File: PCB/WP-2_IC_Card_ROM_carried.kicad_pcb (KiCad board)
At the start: 2 copper layers, 14.5 x 48.5 mm, 6 parts, among them J1 Conn_01x38_Female, U1 FLASH 256Kx8 5v Parallel, U2 FLASH 256Kx8 5v Parallel

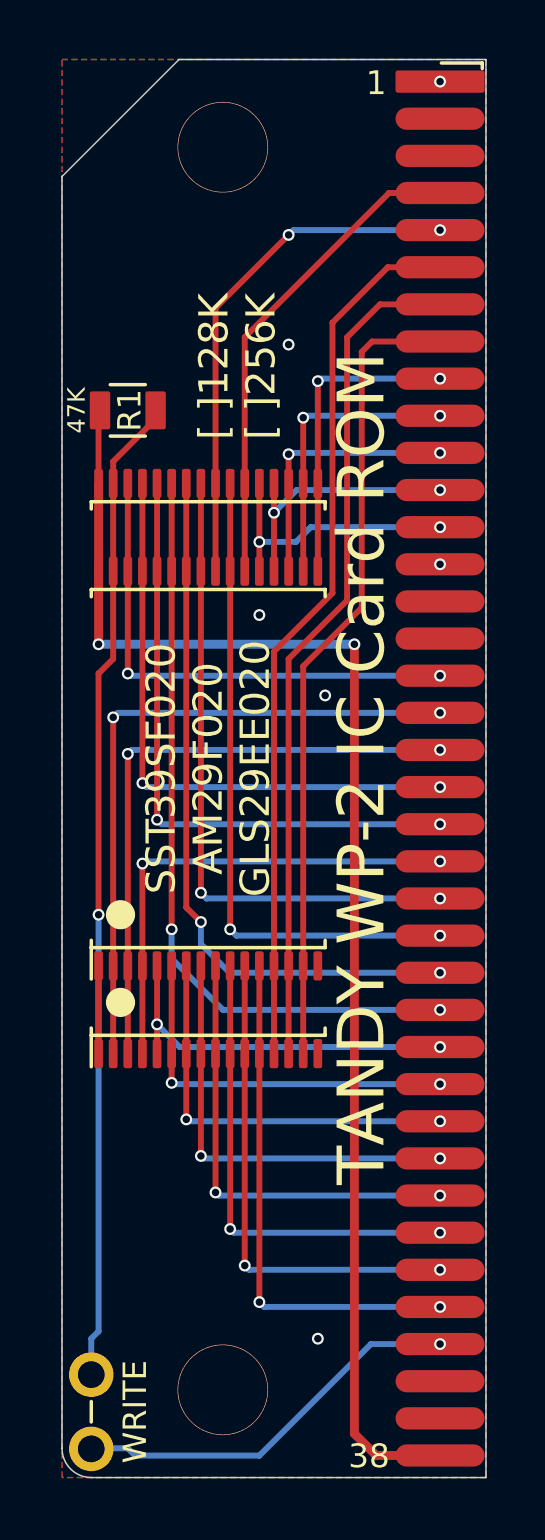
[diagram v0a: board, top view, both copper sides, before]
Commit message: fix ROM flash chip pinout
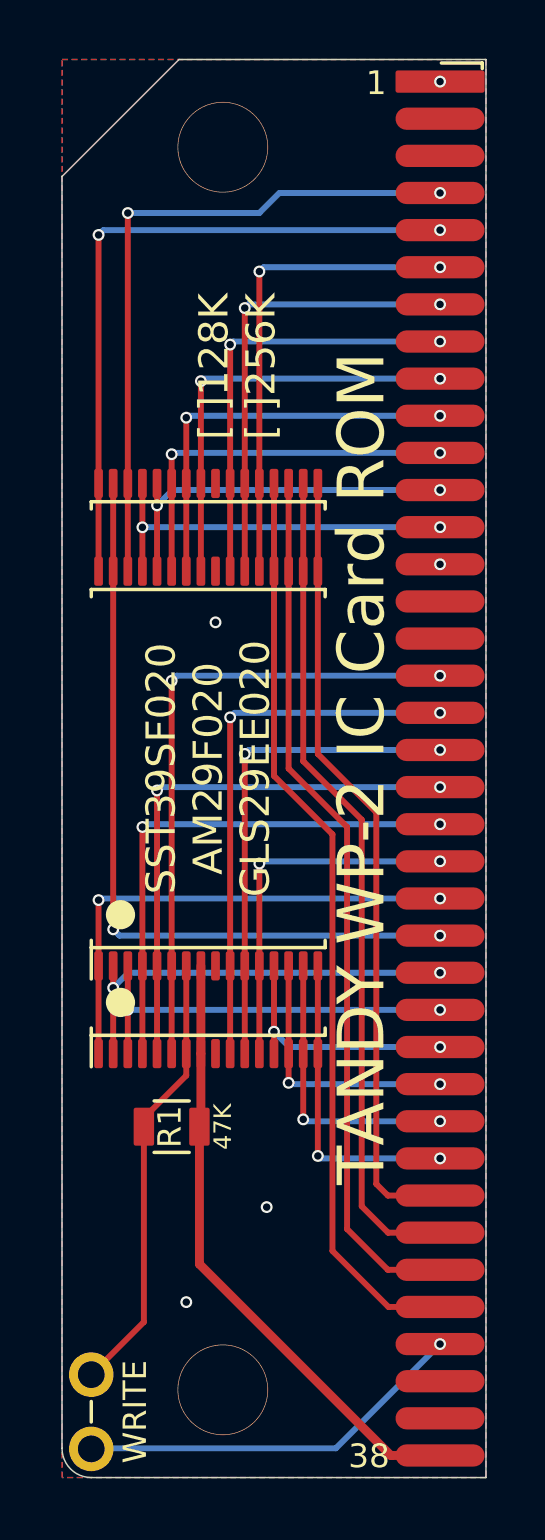
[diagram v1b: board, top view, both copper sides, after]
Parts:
- JP1: value WR_EN -> Write-Enable
- moved R1 24.5 mm to (148.0, 111.9), turned to 180 degrees
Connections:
- U1 pad 1: (no net) -> /A11
- U1 pad 10: /A2 -> /A16
- U1 pad 11: /A1 -> /A15
- U1 pad 12: /A0 -> /A12
- U1 pad 13: /D0 -> /A7
- U1 pad 14: /D1 -> /A6
- U1 pad 15: /D2 -> /A5
- U1 pad 16: GND -> /A4
- U1 pad 17: /D3 -> /A3
- U1 pad 18: /D4 -> /A2
- U1 pad 19: /D5 -> /A1
- U1 pad 2: /A16 -> /A9
- U1 pad 20: /D6 -> /A0
- U1 pad 21: /D7 -> /D0
- U1 pad 22: /~CE1 -> /D1
- U1 pad 23: /A10 -> /D2
- U1 pad 24: /~OE -> GND
- U1 pad 25: /A11 -> /D3
- U1 pad 26: /A9 -> /D4
- U1 pad 27: /A8 -> /D5
- U1 pad 28: /A13 -> /D6
- U1 pad 29: /A14 -> /D7
- U1 pad 3: /A15 -> /A8
- U1 pad 30: /A17 -> /~CE1
- U1 pad 31: /~WE -> /A10
- U1 pad 32: VDD -> /~OE
- U1 pad 4: /A12 -> /A13
- U1 pad 5: /A7 -> /A14
- U1 pad 6: /A6 -> /A17
- U1 pad 7: /A5 -> /~WE
- U1 pad 8: /A4 -> VDD
- U1 pad 9: /A3 -> (no net)
- U2 pad 1: (no net) -> /A11
- U2 pad 10: /A2 -> /A16
- U2 pad 11: /A1 -> /A15
- U2 pad 12: /A0 -> /A12
- U2 pad 13: /D0 -> /A7
- U2 pad 14: /D1 -> /A6
- U2 pad 15: /D2 -> /A5
- U2 pad 16: GND -> /A4
- U2 pad 17: /D3 -> /A3
- U2 pad 18: /D4 -> /A2
- U2 pad 19: /D5 -> /A1
- U2 pad 2: /A16 -> /A9
- U2 pad 20: /D6 -> /A0
- U2 pad 21: /D7 -> /D0
- U2 pad 22: /~CE1 -> /D1
- U2 pad 23: /A10 -> /D2
- U2 pad 24: /~OE -> GND
- U2 pad 25: /A11 -> /D3
- U2 pad 26: /A9 -> /D4
- U2 pad 27: /A8 -> /D5
- U2 pad 28: /A13 -> /D6
- U2 pad 29: /A14 -> /D7
- U2 pad 3: /A15 -> /A8
- U2 pad 30: /A17 -> /~CE1
- U2 pad 31: /~WE -> /A10
- U2 pad 32: VDD -> /~OE
- U2 pad 4: /A12 -> /A13
- U2 pad 5: /A7 -> /A14
- U2 pad 6: /A6 -> /A17
- U2 pad 7: /A5 -> /~WE
- U2 pad 8: /A4 -> VDD
- U2 pad 9: /A3 -> (no net)
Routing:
- net VDD: track 47.0 -> 21.2 mm, vias 2 -> 0
- net /~WE: track 33.9 -> 15.3 mm, vias 1 -> 0
- net /D0: track 30.3 -> 16.5 mm, vias 0 -> 2
- net /A0: track 17.7 -> 31.6 mm, vias 2 -> 0
- net /D1: track 29.0 -> 15.7 mm, vias 0 -> 2
- net /A1: track 17.0 -> 30.1 mm, vias 2 -> 0
- net /D2: track 27.7 -> 15.0 mm, vias 0 -> 2
- net /A8: track 26.2 -> 13.7 mm
- net /A2: track 16.2 -> 28.6 mm, vias 2 -> 0
- net /A3: track 15.5 -> 27.1 mm, vias 2 -> 0
- net /A9: track 24.5 -> 14.4 mm
- net /~CE1: track 16.7 -> 23.2 mm, vias 0 -> 2
- net /~OE: track 17.8 -> 23.2 mm
- net /A11: track 22.3 -> 17.0 mm
- net /A17: track 17.2 -> 22.0 mm
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
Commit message: fine-tune via-near-trace placements
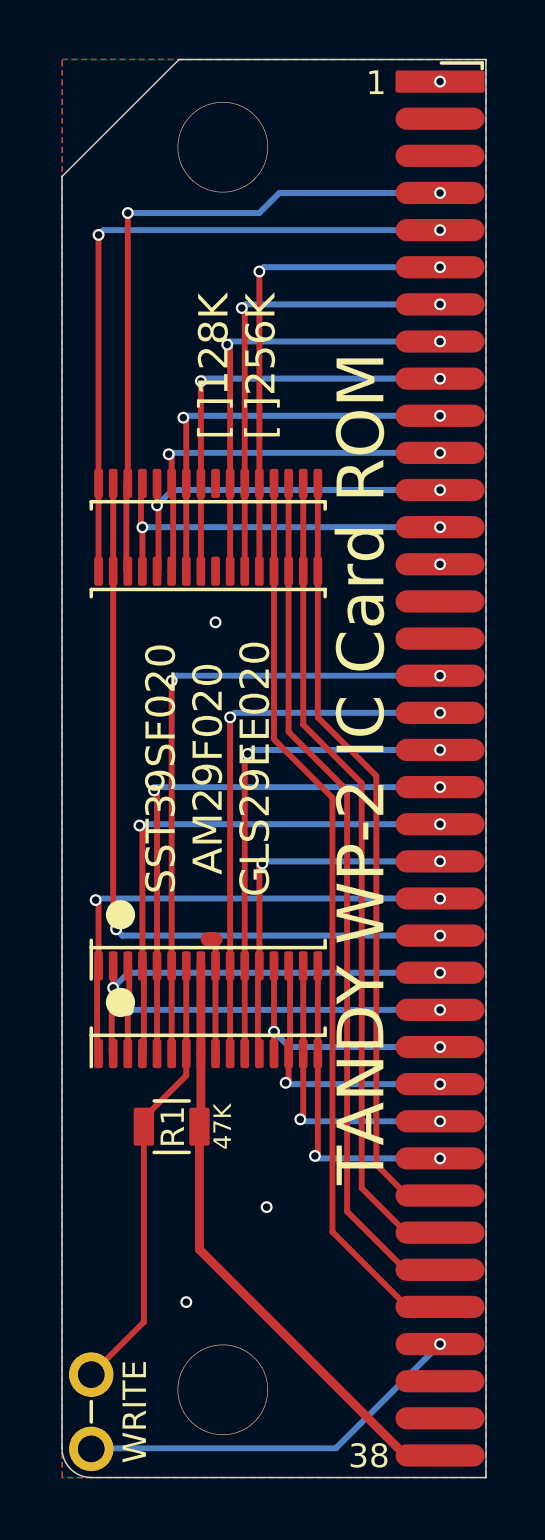
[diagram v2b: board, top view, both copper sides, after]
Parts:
- added NT1: Net-Tie_2, 0_LOCAL:Net_Tie_2p_8mil, F.Cu at (149.5, 105.9)
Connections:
- U1 pad 9: (no net) -> /A18
- U2 pad 9: (no net) -> /A18
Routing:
- net /A18: track 0.00 -> 3.00 mm

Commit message: increase via sizes and min soldermask width for PCBWAY
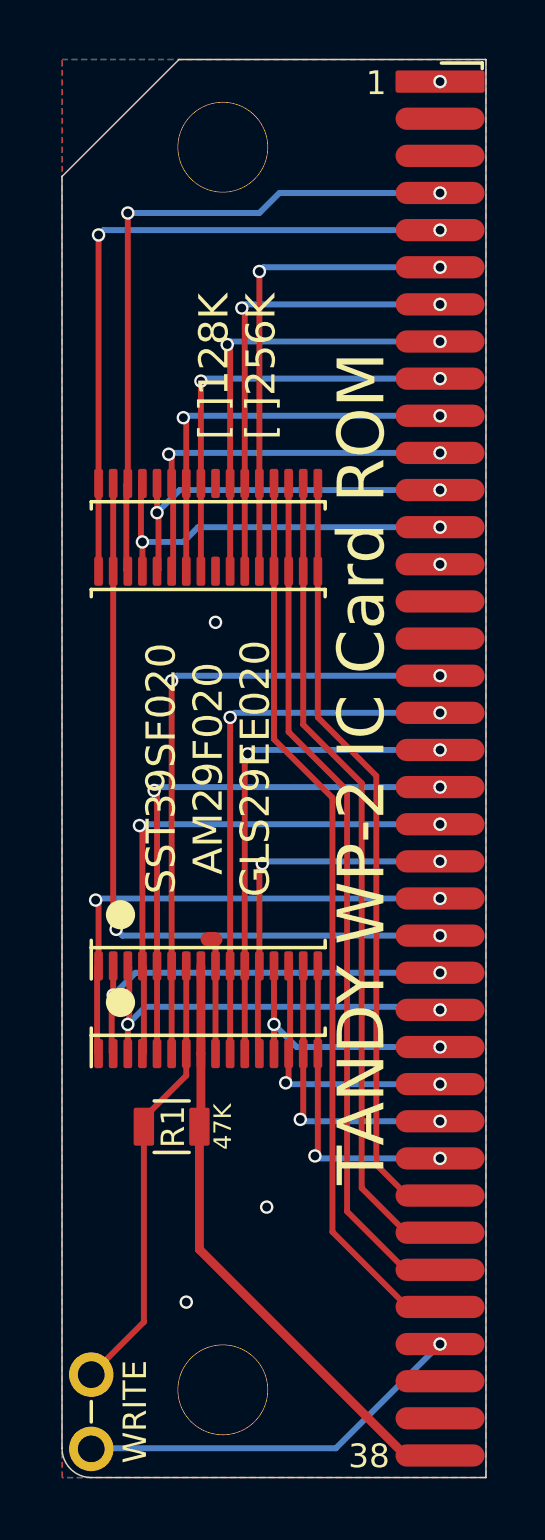
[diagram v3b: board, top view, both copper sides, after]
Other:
- net class Default: clearance 0.1524 -> 0.16; trace_width 0.254 -> 0.18; via_dia 0.4064 -> 0.46; via_drill 0.254 -> 0.3
- rule trace_clearance: 0.1524 -> 0.16
- rule via_min_drill: 0.254 -> 0.3
- rule via_min_size: 0.4064 -> 0.46
